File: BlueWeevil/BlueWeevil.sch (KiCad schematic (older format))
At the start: 197 parts

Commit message: 1st pass at layout. Needs packages verified, and underglow LEDs added
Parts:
- RP1: renamed from RP?; footprint (none) -> Resistors_SMD:R_Array_Convex_4x1206
- U1: renamed from U?; footprint (none) -> Housings_SSOP:SSOP-28_5.3x10.2mm_Pitch0.65mm
- gave numbers to parts that had none: 39
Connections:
- net CA1: now also SW_F7_52.A, SW_F9_67.A; no longer SW_U_28.A, SW_X11Y1_10.A
- net CA2: now also SW_E_24.K, SW_F10_68.A, SW_F8_53.A, SW_Q_22.K, SW_R_25.K, SW_T_26.K, SW_Tab_21.K, SW_W_23.K; no longer SW_Backspace_16.K, SW_I_29.A, SW_Ins_17.K, SW_X12Y1_11.A, SW_X13Y1_12.K, SW_X14Y1_13.K, SW_X15Y1_14.K, SW_X16Y1_15.K
- net CA3: now also SW_A_40.K, SW_Ctrl_69.A, SW_D_42.K, SW_F3_19.K, SW_F4_20.K, SW_F_43.K, SW_G_44.K, SW_S_41.K, SW_Shift_54.A; no longer SW_E_24.K, SW_O_30.A, SW_Q_22.K, SW_R_25.K, SW_T_26.K, SW_W_23.K, SW_X11Y1_10.K, SW_X12Y1_11.K, SW_X13Y1_12.A
- net CA4: now also SW_B_59.K, SW_C_57.K, SW_Caps_39.K, SW_F5_37.K, SW_F6_38.K, SW_V_58.K, SW_Win_70.A, SW_X_56.K, SW_Z_55.A; no longer SW_Del_35.K, SW_F3_19.K, SW_F4_20.K, SW_P_31.A, SW_Tab_21.K, SW_X14Y1_13.A, SW_X15Y2_32.K, SW_X16Y2_33.K, SW_X17Y2_34.K
- net CA5: now also SW_Alt_71.A, SW_F7_52.K, SW_F8_53.K, SW_Shift_54.K, SW_X8Y5_72.K, SW_X_56.A, SW_Z_55.K; no longer SW_D_42.K, SW_F_43.K, SW_G_44.K, SW_I_29.K, SW_O_30.K, SW_P_31.K, SW_U_28.K, SW_X15Y1_14.A, SW_X15Y2_32.A
- net CA6: now also SW_Alt_71.K, SW_C_57.A, SW_Ctrl_69.K, SW_F10_68.K, SW_F9_67.K, SW_Win_70.K, SW_X8Y5_72.A; no longer SW_A_40.K, SW_Caps_39.K, SW_F5_37.K, SW_F6_38.K, SW_S_41.K, SW_X16Y1_15.A, SW_X16Y2_33.A
- net CA7: now also RGB10.4 (B), RGB11.4 (B), RGB12.4 (B), RGB13.4 (B), RGB14.4 (B), RGB15.4 (B), SW_V_58.A; no longer RGB10.2 (R), RGB11.2 (R), RGB12.2 (R), RGB13.2 (R), RGB14.2 (R), RGB15.2 (R), SW_Backspace_16.A, SW_X17Y2_34.A
- net CA8: now also SW_B_59.A; no longer SW_Del_35.A, SW_Ins_17.A
- net CA9: now also RGB10.2 (R), RGB11.2 (R), RGB12.2 (R), RGB13.2 (R), RGB14.2 (R), RGB15.2 (R); no longer RGB10.4 (B), RGB11.4 (B), RGB12.4 (B), RGB13.4 (B), RGB14.4 (B), RGB15.4 (B)
- net CB1: now also SW_Backspace_16.K, SW_H_45.A, SW_N_60.A, SW_X11Y1_10.K, SW_X12Y1_11.K, SW_X13Y1_12.K, SW_X14Y1_13.K, SW_X15Y1_14.K, SW_X16Y1_15.K, SW_Y_27.A; no longer SW_F7_52.K, SW_F8_53.K, SW_J_46.K, SW_PgDn_36.K, SW_PgUp_18.K, SW_Shift_54.K, SW_V_58.A, SW_X19Y4_66.A, SW_Y_27.K, SW_Z_55.A
- net CB2: now also SW_I_29.K, SW_M_61.A, SW_O_30.K, SW_P_31.K, SW_U_28.A, SW_X11Y1_10.A, SW_X15Y2_32.K, SW_X16Y2_33.K, SW_X17Y2_34.K; no longer SW_B_59.A, SW_C_57.K, SW_F9_67.A, SW_K_47.A, SW_L_48.K, SW_Shift_65.K, SW_X15Y3_49.K, SW_X15Y4_64.K, SW_X_56.K
- net CB3: now also SW_Enter_51.K, SW_I_29.A, SW_K_47.A, SW_L_48.K, SW_PgDn_36.K, SW_U_28.K, SW_X12Y1_11.A, SW_X13Y4_62.A, SW_X15Y3_49.K, SW_X16Y3_50.K, SW_Y_27.K; no longer SW_Alt_71.K, SW_Ctrl_69.K, SW_F10_68.A, SW_F8_53.A, SW_H_45.K, SW_K_47.K, SW_L_48.A, SW_N_60.A, SW_Win_70.K, SW_X8Y5_72.K, SW_Z_55.K
- net CB4: now also SW_H_45.K, SW_J_46.K, SW_K_47.K, SW_L_48.A, SW_O_30.A, SW_PgUp_18.K, SW_Shift_65.K, SW_X13Y1_12.A, SW_X14Y4_63.A, SW_X15Y4_64.K; no longer SW_Ctrl_69.A, SW_F10_68.K, SW_F9_67.K, SW_M_61.A, SW_Shift_54.A, SW_X15Y3_49.A, SW_X16Y3_50.K, SW_X19Y5_77.K, SW_X20Y5_78.K
- net CB5: now also SW_Del_35.K, SW_Ins_17.K, SW_M_61.K, SW_N_60.K, SW_P_31.A, SW_X13Y4_62.K, SW_X14Y1_13.A, SW_X15Y3_49.A, SW_X20Y5_78.K; no longer SW_Alt_73.K, SW_Enter_51.K, SW_F7_52.A, SW_Menu_75.K, SW_Win_70.A, SW_Win_74.K, SW_X13Y4_62.A, SW_X18Y5_76.K
- net CB6: now also SW_Alt_73.K, SW_Menu_75.K, SW_Win_74.K, SW_X15Y1_14.A, SW_X15Y2_32.A, SW_X16Y3_50.A, SW_X18Y5_76.K, SW_X19Y5_77.K; no longer SW_Alt_71.A, SW_B_59.K, SW_M_61.K, SW_N_60.K, SW_PgUp_18.A, SW_V_58.K, SW_X13Y4_62.K, SW_X14Y4_63.A
- net CB7: now also RGB20.4 (B), RGB21.4 (B), RGB22.4 (B), RGB23.4 (B), RGB24.4 (B), RGB25.4 (B), SW_Ins_17.A, SW_X16Y1_15.A, SW_X16Y2_33.A, SW_X19Y4_66.A; no longer RGB20.2 (R), RGB21.2 (R), RGB22.2 (R), RGB23.2 (R), RGB24.2 (R), RGB25.2 (R), SW_PgDn_36.A, SW_X16Y3_50.A, SW_X8Y5_72.A, SW_X_56.A
- net CB8: now also SW_Backspace_16.A, SW_Del_35.A, SW_PgDn_36.A, SW_PgUp_18.A, SW_X17Y2_34.A; no longer SW_C_57.A, SW_H_45.A, SW_Y_27.A
- net CB9: now also RGB20.2 (R), RGB21.2 (R), RGB22.2 (R), RGB23.2 (R), RGB24.2 (R), RGB25.2 (R); no longer RGB20.4 (B), RGB21.4 (B), RGB22.4 (B), RGB23.4 (B), RGB24.4 (B), RGB25.4 (B)
- net LED_SDA: now also RP1.6 (R3); no longer RP1.8 (R1)
- net USB-: now reaches J1.2 (D-), R6.2
- net USB+: now reaches J1.3 (D+), R7.2
- net at U1.4 (INTB): now also RP1.8 (R1); no longer RP1.6 (R3)
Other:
- moved on the sheet: SW_A_40B, SW_Alt_71B, SW_Alt_73B, SW_B_59B, SW_Backspace_16B, SW_C_57B, SW_Caps_39B, SW_Ctrl_69B, SW_D_42B, SW_Del_35B, SW_E_24B, SW_Enter_51B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

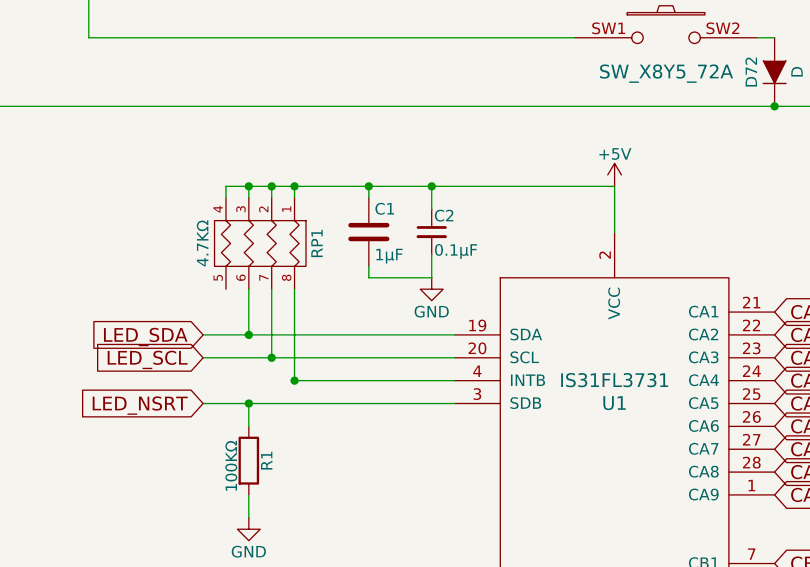
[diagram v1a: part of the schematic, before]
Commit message: Packages verified, BOM w/part numbers created
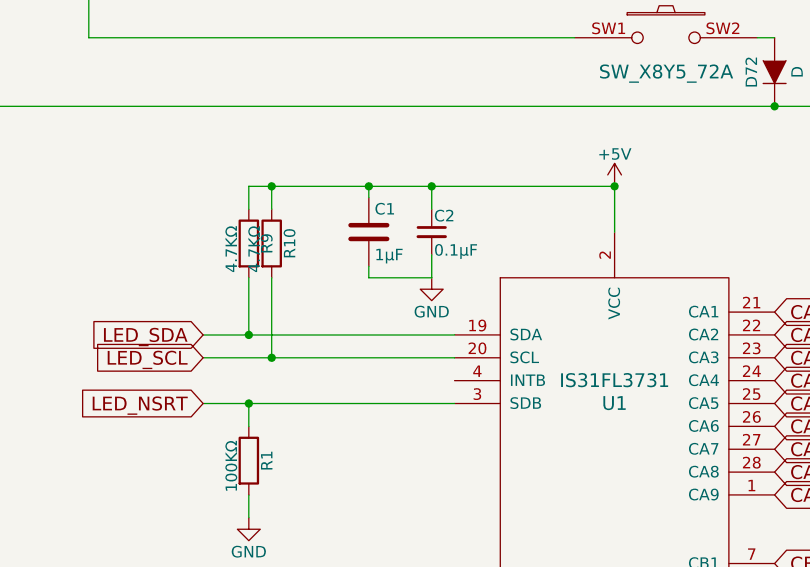
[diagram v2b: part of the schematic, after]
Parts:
- removed RP1: 4.7KΩ, Resistors_SMD:R_Array_Convex_4x1206, symbol R_PACK4
- added R10, R9: 4.7KΩ, Resistors_SMD:R_1206_HandSoldering, symbol R
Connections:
- net +5V: now also R10.1, R9.1
- net LED_SCL: now also R10.2
- net LED_SDA: now also R9.2
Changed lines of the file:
@@
 LED_SCL
-$Comp
-L R_PACK4 RP1
-U 1 1 578F53DB
-P 8750 6500
-F 0 "RP1" H 8750 6950 50  0000 C CNN
-F 1 "4.7KΩ" H 8750 6450 50  0000 C CNN
-F 2 "Resistors_SMD:R_Array_Convex_4x1206" H 8750 6500 50  0001 C CNN
-F 3 "" H 8750 6500 50  0000 C CNN
-	1    8750 6500
-	0    1    1    0
-$EndComp
 $Comp
 L R R1
@@
 	9425 6250 9425 6300
 Wire Wire Line
-	8800 6250 10500 6250
-Wire Wire Line
 	9700 6250 9700 6350
 Wire Wire Line
@@
 Connection ~ 9650 8850
 Wire Wire Line
-	8900 6300 8900 6250
+	8900 6250 8900 6350
 Connection ~ 9425 6250
 Wire Wire Line
-	9000 6300 9000 6250
+	9000 6250 9000 6350
 Connection ~ 9000 6250
 Wire Wire Line
-	9100 6300 9100 6250
-Connection ~ 9100 6250
-Wire Wire Line
-	8800 6300 8800 6250
-Connection ~ 8900 6250
-Wire Wire Line
 	8700 6900 9800 6900
 Wire Wire Line
 	8700 7000 9800 7000
 Wire Wire Line
-	9100 6700 9100 7100
-Wire Wire Line
-	9000 7000 9000 6700
+	9000 6650 9000 7000
 Connection ~ 9000 7000
 Wire Wire Line
@@
 	5300 15100 5100 15100
 Connection ~ 5100 15100
-Connection ~ 9100 7100
-Wire Wire Line
-	9100 7100 9800 7100
-Wire Wire Line
-	8900 6900 8900 6700
+Wire Wire Line
+	8900 6650 8900 6900
 Connection ~ 8900 6900
+$Comp
+L R R9
+U 1 1 57950653
+P 8900 6500
+F 0 "R9" V 8980 6500 50  0000 C CNN
+F 1 "4.7KΩ" V 8825 6475 50  0000 C CNN
+F 2 "Resistors_SMD:R_1206_HandSoldering" V 8830 6500 50  0001 C CNN
+F 3 "" H 8900 6500 50  0000 C CNN
+	1    8900 6500
+	1    0    0    -1
+$EndComp
+$Comp
+L R R10
+U 1 1 579509B4
+P 9000 6500
+F 0 "R10" V 9080 6500 50  0000 C CNN
+F 1 "4.7KΩ" V 8925 6475 50  0000 C CNN
+F 2 "Resistors_SMD:R_1206_HandSoldering" V 8930 6500 50  0001 C CNN
+F 3 "" H 9000 6500 50  0000 C CNN
+	1    9000 6500
+	1    0    0    -1
+$EndComp
+Wire Wire Line
+	8900 6250 10500 6250
+Connection ~ 10500 6250
 $EndSCHEMATC
